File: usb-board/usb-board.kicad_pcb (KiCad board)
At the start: 2 copper layers, 30 x 17.5 mm, 14 parts, among them J1 Conn_01x06, J2 USB_C_Receptacle_USB2.0

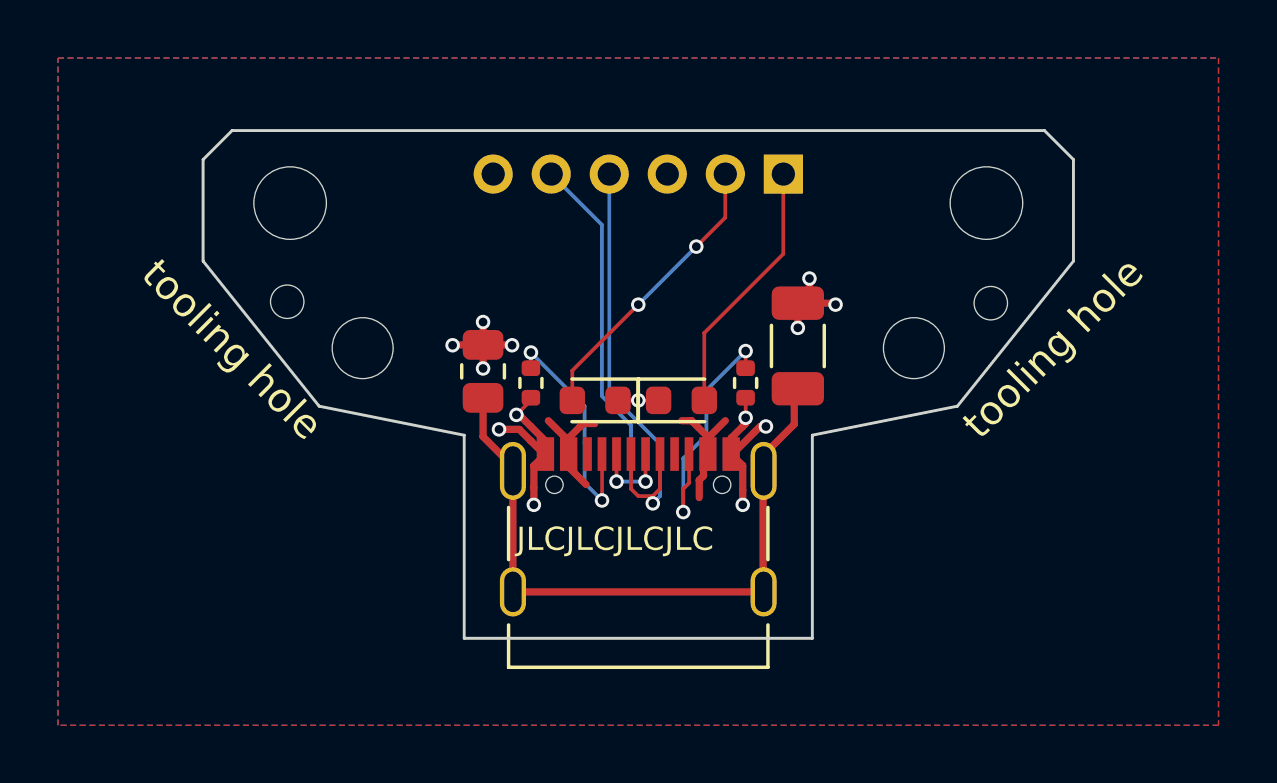
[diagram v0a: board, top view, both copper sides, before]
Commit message: usb-board: improve VBUS connection
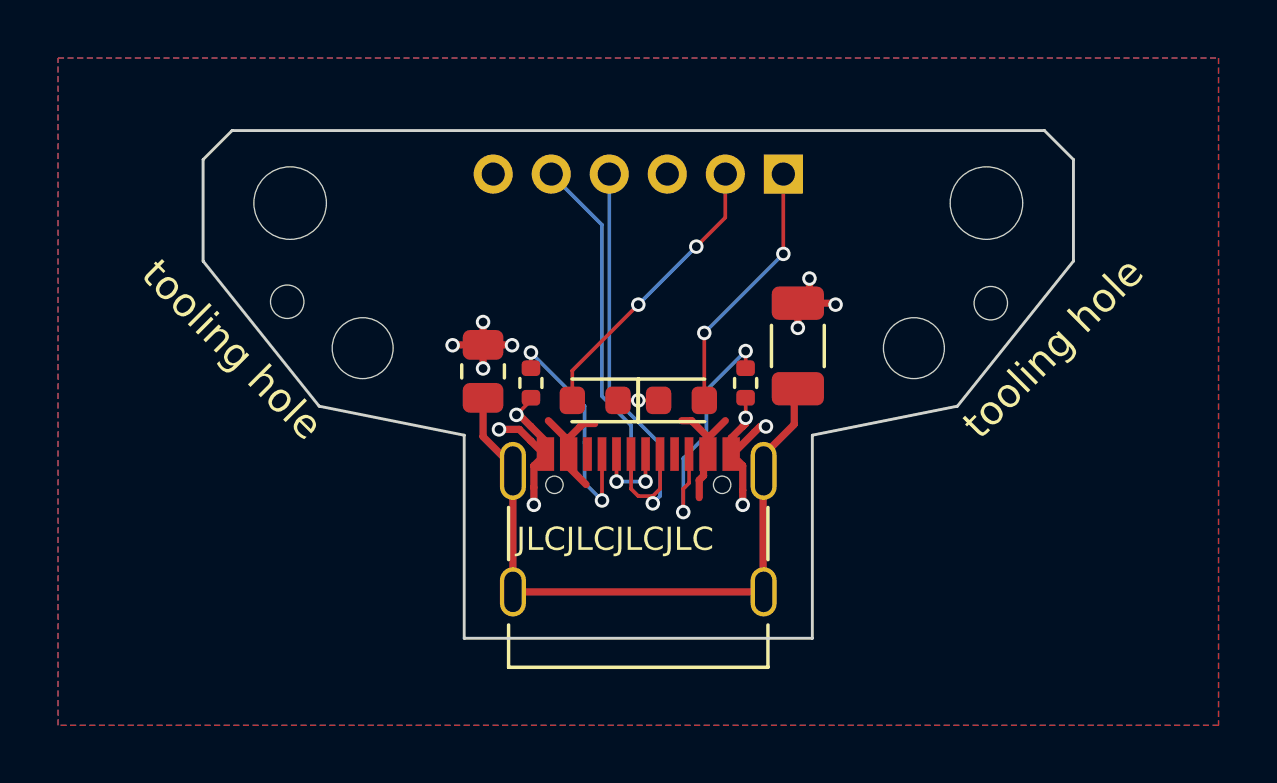
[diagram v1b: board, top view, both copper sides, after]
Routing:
- net Net-(D2-A): vias 0 -> 2
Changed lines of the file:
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@@
   (segment (start 100 98.5) (end 102 96.5) (width 0.127) (layer "B.Cu") (net 3))
   (segment (start 105 96.75) (end 105 93.95) (width 0.127) (layer "F.Cu") (net 4))
-  (segment (start 102.275002 99.474998) (end 105 96.75) (width 0.127) (layer "F.Cu") (net 4))
+  (segment (start 102.275002 99.474998) (end 102.275 99.475) (width 0.127) (layer "F.Cu") (net 4))
   (segment (start 102.275002 101.8) (end 102.275002 99.474998) (width 0.127) (layer "F.Cu") (net 4))
+  (via (at 102.275 99.475) (size 0.5) (drill 0.3) (layers "F.Cu" "B.Cu") (net 4))
+  (via (at 105 96.75) (size 0.5) (drill 0.3) (layers "F.Cu" "B.Cu") (net 4))
+  (segment (start 102.275 99.475) (end 105 96.75) (width 0.127) (layer "B.Cu") (net 4))
   (segment (start 99.75 103.65) (end 99.75 104.85) (width 0.127) (layer "F.Cu") (net 5))
   (segment (start 100 105.1) (end 100.5 105.1) (width 0.127) (layer "F.Cu") (net 5))

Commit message: usb-board: add silkscreen markings
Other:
- board text added: "Blinkekatze USB board Rev 1.0 2023"

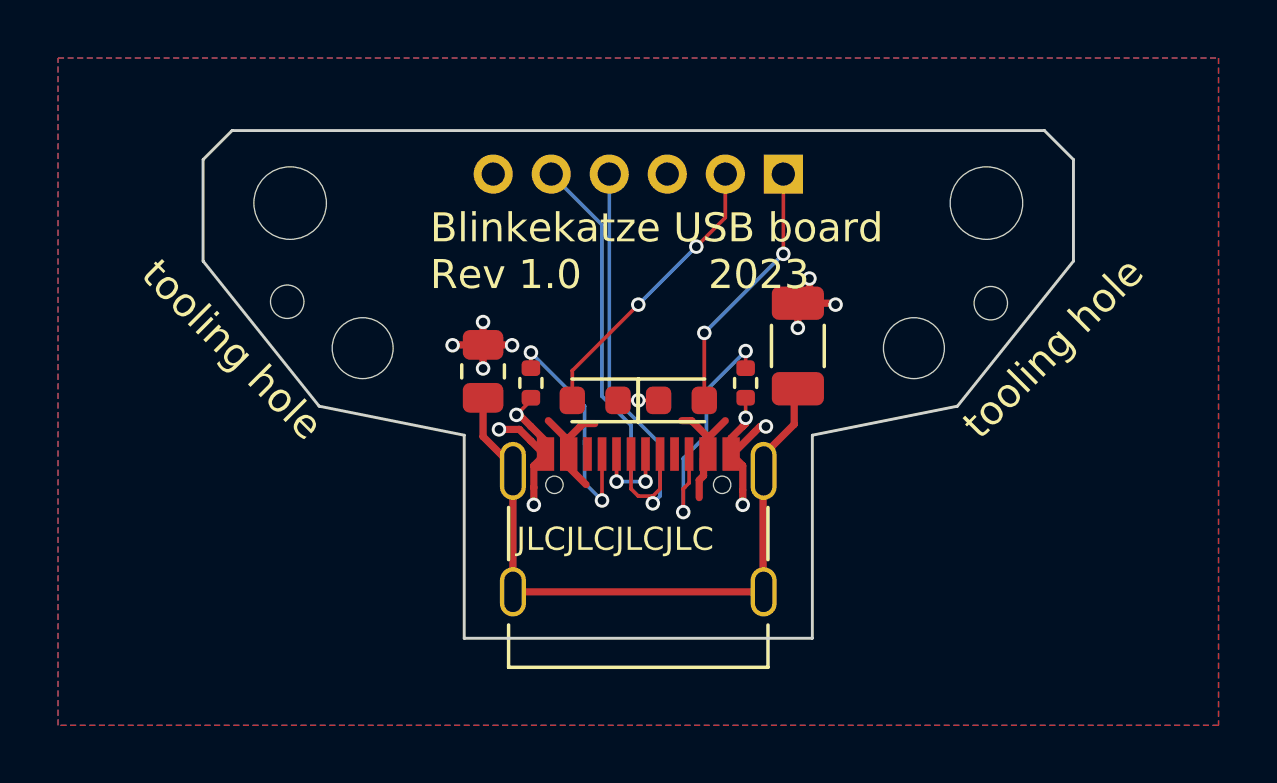
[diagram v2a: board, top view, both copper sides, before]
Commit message: Change mainboard connector to FFC type
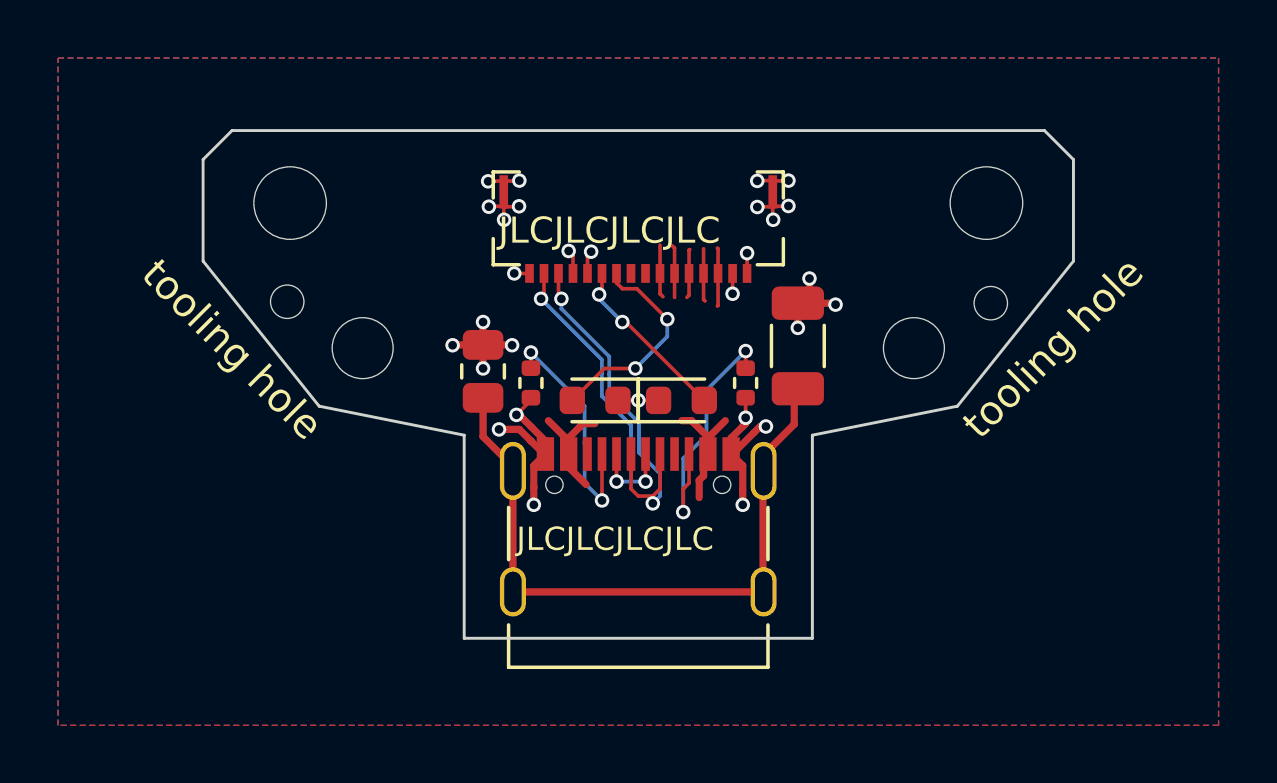
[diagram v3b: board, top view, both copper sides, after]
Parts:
- removed J1: Conn_01x06, Connector_PinHeader_2.00mm:PinHeader_1x06_P2.00mm_Vertical
- added J3: Mainboard, Connector_FFC-FPC_HDGC:0.5K-QX-16PWB_16Pin_0.5mm, F.Cu at (100.0, 97.4)
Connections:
- net VBUS renamed Net-(J3-Pin_3)
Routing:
- net GND: track 20.5 -> 30.7 mm, vias 14 -> 29
- net Net-(J3-Pin_3): track 9.59 -> 18.7 mm
- net Net-(J3-Pin_15): track 14.6 -> 11.4 mm, vias 2 -> 3
- net Net-(D2-A): track 8.98 -> 5.99 mm
- net Net-(J3-Pin_14): track 16.0 -> 13.4 mm, vias 1 -> 2
- net Net-(D1-A): track 9.98 -> 7.38 mm
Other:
- board text added: "2023"
- board text added: "Blinkekatze USB board"
- board text added: "Rev 1.0"
- board text removed: "Blinkekatze USB board Rev 1.0 2023"
- board text removed: "D+"
- board text removed: "D-"
- board text removed: "GND"
- board text removed: "LED1"
- board text removed: "LED2"
- board text removed: "VBUS"

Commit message: usb-board: fix FFC pinout
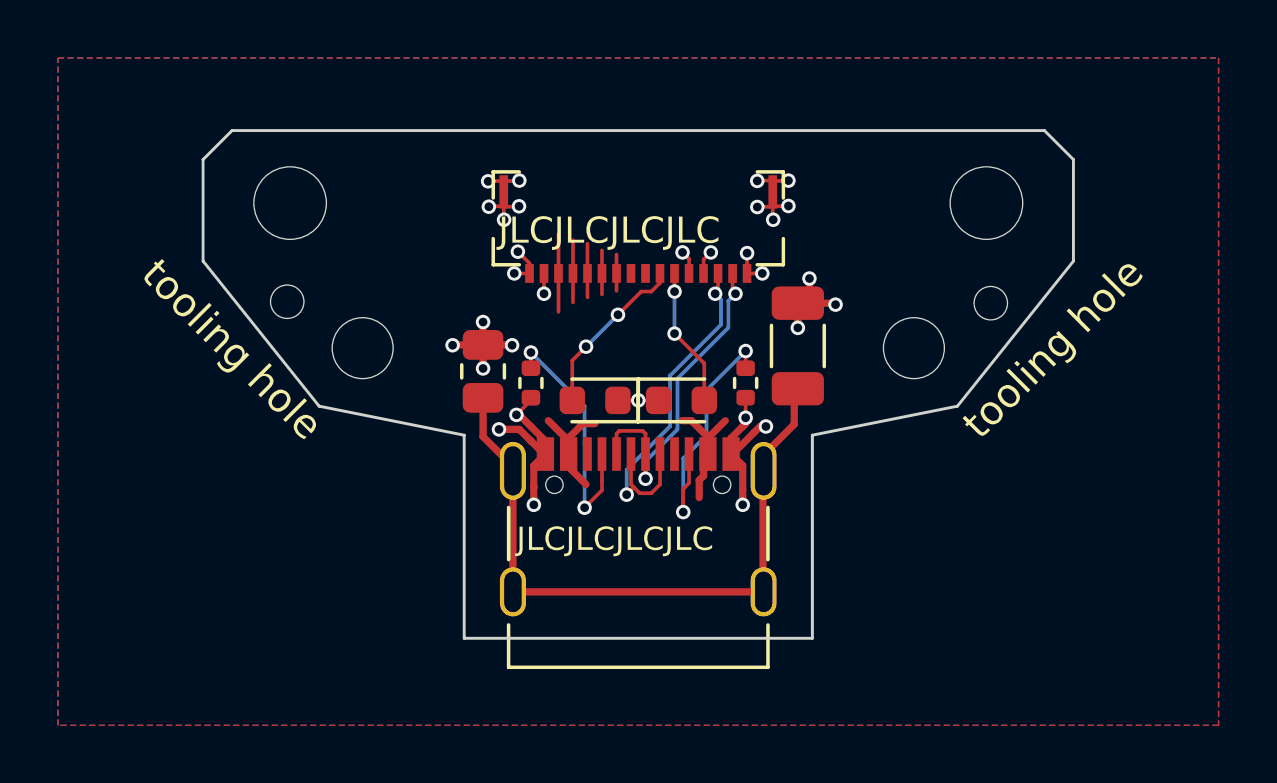
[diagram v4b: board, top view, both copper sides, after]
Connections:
- J2 pad A4: Net-(J3-Pin_3) -> Net-(J3-Pin_10)
- J2 pad A6: Net-(J3-Pin_14) -> Net-(J3-Pin_3)
- J2 pad A7: Net-(J3-Pin_15) -> Net-(J3-Pin_2)
- J2 pad A9: Net-(J3-Pin_3) -> Net-(J3-Pin_10)
- J2 pad B4: Net-(J3-Pin_3) -> Net-(J3-Pin_10)
- J2 pad B6: Net-(J3-Pin_14) -> Net-(J3-Pin_3)
- J2 pad B7: Net-(J3-Pin_15) -> Net-(J3-Pin_2)
- J2 pad B9: Net-(J3-Pin_3) -> Net-(J3-Pin_10)
- J3 pad 10: Net-(D1-A) -> Net-(J3-Pin_10)
- J3 pad 11: Net-(D2-A) -> Net-(J3-Pin_10)
- J3 pad 12: GND -> Net-(J3-Pin_10)
- J3 pad 13: GND -> Net-(J3-Pin_10)
- J3 pad 14: Net-(J3-Pin_14) -> Net-(J3-Pin_10)
- J3 pad 15: Net-(J3-Pin_15) -> GND
- J3 pad 2: GND -> Net-(J3-Pin_2)
- J3 pad 4: Net-(J3-Pin_3) -> GND
- J3 pad 5: Net-(J3-Pin_3) -> GND
- J3 pad 6: Net-(J3-Pin_3) -> Net-(D2-A)
- J3 pad 7: Net-(J3-Pin_3) -> Net-(D1-A)
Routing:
- net Net-(J3-Pin_10): track 0.00 -> 19.1 mm
- net Net-(J3-Pin_14): track 13.4 -> 0.00 mm, vias 2 -> 0
- net Net-(J3-Pin_2): track 0.00 -> 11.7 mm, vias 0 -> 2
- net Net-(J3-Pin_15): track 11.4 -> 0.00 mm, vias 3 -> 0
- net Net-(J3-Pin_3): track 18.7 -> 12.8 mm, vias 0 -> 2
- net Net-(D1-A): track 7.38 -> 5.83 mm
- net GND: track 30.7 -> 32.1 mm, vias 29 -> 31
- net Net-(D2-A): track 5.99 -> 4.82 mm
- net Net-(J2-CC1): track 8.41 -> 8.91 mm
- added copper zone on F.Cu, net Net-(J3-Pin_10)
- removed copper zone on F.Cu, net Net-(J3-Pin_3)

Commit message: usb-board: update silkscreen designators
- Remove second JLCJLCJLCJLC designator
- Change revision indicator to Rev2.0
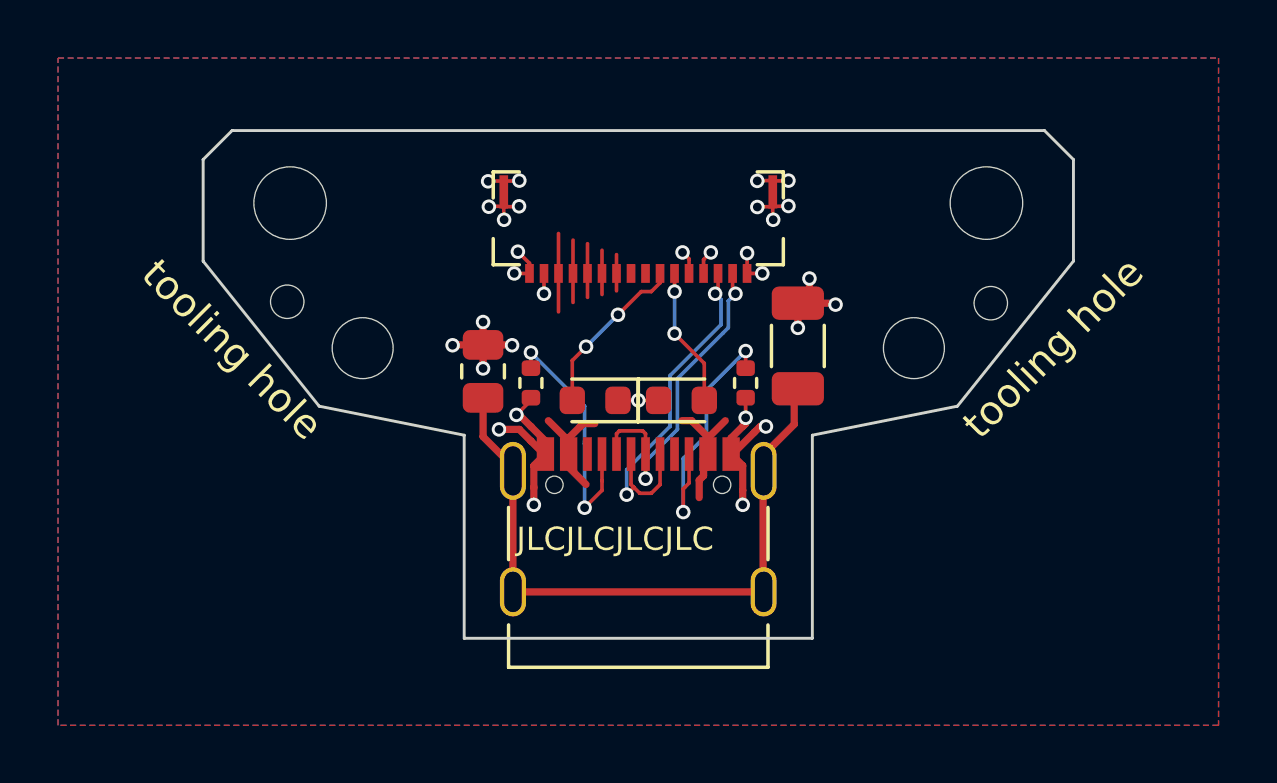
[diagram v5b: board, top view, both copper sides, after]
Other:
- board text added: "Rev 2.0"
- board text removed: "Rev 1.0"
